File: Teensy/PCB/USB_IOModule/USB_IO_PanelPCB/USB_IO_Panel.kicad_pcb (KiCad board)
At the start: 2 copper layers, 61 x 128 mm, 31 parts, among them J1 USB_B, J2 USB_A

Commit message: Generated Gerbers
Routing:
- added copper zone on B.Cu, net shielding
- added copper zone on F.Cu, net shielding
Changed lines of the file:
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@@
       (layerselection 0x00010fc_ffffffff)
       (disableapertmacros false)
-      (usegerberextensions false)
-      (usegerberattributes true)
-      (usegerberadvancedattributes true)
-      (creategerberjobfile true)
+      (usegerberextensions true)
+      (usegerberattributes false)
+      (usegerberadvancedattributes false)
+      (creategerberjobfile false)
       (svguseinch false)
       (svgprecision 6)
@@
       (psa4output false)
       (plotreference true)
-      (plotvalue true)
+      (plotvalue false)
       (plotinvisibletext false)
       (sketchpadsonfab false)
-      (subtractmaskfromsilk false)
+      (subtractmaskfromsilk true)
       (outputformat 1)
       (mirror false)
-      (drillshape 1)
+      (drillshape 0)
       (scaleselection 1)
-      (outputdirectory "")
+      (outputdirectory "USB_IO_Panel_Gerber")
     )
   )
   (net 0 "")
+  (net 1 "shielding")
   (footprint "Potentiometer:Bourns_PTV09A-X_Hole" (layer "F.Cu")
     (at 91.435 157.48)
@@
     (fp_line (start -2.54 -64) (end 2.54 -64) (layer "User.1") (width 0.12))
     (fp_circle (center 0 0) (end 0 0) (layer "User.1") (width 0.12) (fill none))
-    (fp_line (start -1.27 -62.85) (end 1.27 -62.85) (layer "User.2") (width 0.12))
-    (fp_line (start -1.27 -59.65) (end 1.27 -59.65) (layer "User.2") (width 0.12))
-    (fp_line (start -1.27 59.65) (end 1.27 59.65) (layer "User.2") (width 0.12))
-    (fp_line (start -1.27 62.85) (end 1.27 62.85) (layer "User.2") (width 0.12))
-    (fp_arc (start -1.27 -59.65) (mid -2.87 -61.25) (end -1.27 -62.85) (layer "User.2") (width 0.12))
-    (fp_arc (start 1.27 59.65) (mid 2.87 61.25) (end 1.27 62.85) (layer "User.2") (width 0.12))
-    (fp_arc (start 1.27 -62.85) (mid 2.87 -61.25) (end 1.27 -59.65) (layer "User.2") (width 0.12))
-    (fp_arc (start -1.27 62.85) (mid -2.87 61.25) (end -1.27 59.65) (layer "User.2") (width 0.12))
-    (pad "" np_thru_hole oval (at 0 61.25) (size 5.74 3.2) (drill oval 5.74 3.2) (layers *.Mask))
-    (pad "" np_thru_hole oval (at 0 -61.25) (size 5.74 3.2) (drill oval 5.74 3.2) (layers *.Mask))
+    (fp_line (start -1.6 -59.65) (end 1.6 -59.65) (layer "User.2") (width 0.12))
+    (fp_line (start -1.6 62.85) (end 1.6 62.85) (layer "User.2") (width 0.12))
+    (fp_line (start -1.6 -62.85) (end 1.6 -62.85) (layer "User.2") (width 0.12))
+    (fp_line (start -1.6 59.65) (end 1.6 59.65) (layer "User.2") (width 0.12))
+    (fp_arc (start 1.6 -62.85) (mid 3.2 -61.25) (end 1.6 -59.65) (layer "User.2") (width 0.12))
+    (fp_arc (start -1.6 -59.65) (mid -3.2 -61.25) (end -1.6 -62.85) (layer "User.2") (width 0.12))
+    (fp_arc (start -1.6 62.85) (mid -3.2 61.25) (end -1.6 59.65) (layer "User.2") (width 0.12))
+    (fp_arc (start 1.6 59.65) (mid 3.2 61.25) (end 1.6 62.85) (layer "User.2") (width 0.12))
+    (pad "1" thru_hole oval (at 0 -61.25) (size 7.4 4.2) (drill oval 6.4 3.2) (layers *.Cu *.Mask)
+      (net 1 "shielding"))
+    (pad "1" thru_hole oval (at 0 61.25) (size 7.4 4.2) (drill oval 6.4 3.2) (layers *.Cu *.Mask)
+      (net 1 "shielding"))
   )
   (footprint "Perfboard:3.5mm Jack Perfboard_Hole" (layer "F.Cu")
@@
       (effects (font (size 1 1) (thickness 0.15)))
     )
+    (fp_line (start -2.54 64) (end 2.54 64) (layer "User.1") (width 0.12))
     (fp_line (start -2.54 -64) (end 2.54 -64) (layer "User.1") (width 0.12))
-    (fp_line (start -2.54 64) (end 2.54 64) (layer "User.1") (width 0.12))
     (fp_circle (center 0 0) (end 0 0) (layer "User.1") (width 0.12) (fill none))
-    (fp_line (start -1.27 59.65) (end 1.27 59.65) (layer "User.2") (width 0.12))
-    (fp_line (start -1.27 -62.85) (end 1.27 -62.85) (layer "User.2") (width 0.12))
-    (fp_line (start -1.27 -59.65) (end 1.27 -59.65) (layer "User.2") (width 0.12))
-    (fp_line (start -1.27 62.85) (end 1.27 62.85) (layer "User.2") (width 0.12))
-    (fp_arc (start 1.27 -62.85) (mid 2.87 -61.25) (end 1.27 -59.65) (layer "User.2") (width 0.12))
-    (fp_arc (start -1.27 -59.65) (mid -2.87 -61.25) (end -1.27 -62.85) (layer "User.2") (width 0.12))
-    (fp_arc (start -1.27 62.85) (mid -2.87 61.25) (end -1.27 59.65) (layer "User.2") (width 0.12))
-    (fp_arc (start 1.27 59.65) (mid 2.87 61.25) (end 1.27 62.85) (layer "User.2") (width 0.12))
-    (pad "" np_thru_hole oval (at 0 -61.25) (size 5.74 3.2) (drill oval 5.74 3.2) (layers *.Mask))
-    (pad "" np_thru_hole oval (at 0 61.25) (size 5.74 3.2) (drill oval 5.74 3.2) (layers *.Mask))
+    (fp_line (start -1.6 59.65) (end 1.6 59.65) (layer "User.2") (width 0.12))
+    (fp_line (start -1.6 -59.65) (end 1.6 -59.65) (layer "User.2") (width 0.12))
+    (fp_line (start -1.6 62.85) (end 1.6 62.85) (layer "User.2") (width 0.12))
+    (fp_line (start -1.6 -62.85) (end 1.6 -62.85) (layer "User.2") (width 0.12))
+    (fp_arc (start -1.6 -59.65) (mid -3.2 -61.25) (end -1.6 -62.85) (layer "User.2") (width 0.12))
+    (fp_arc (start 1.6 59.65) (mid 3.2 61.25) (end 1.6 62.85) (layer "User.2") (width 0.12))
+    (fp_arc (start -1.6 62.85) (mid -3.2 61.25) (end -1.6 59.65) (layer "User.2") (width 0.12))
+    (fp_arc (start 1.6 -62.85) (mid 3.2 -61.25) (end 1.6 -59.65) (layer "User.2") (width 0.12))
+    (pad "1" thru_hole oval (at 0 61.25) (size 7.4 4.2) (drill oval 6.4 3.2) (layers *.Cu *.Mask)
+      (net 1 "shielding"))
+    (pad "1" thru_hole oval (at 0 -61.25) (size 7.4 4.2) (drill oval 6.4 3.2) (layers *.Cu *.Mask)
+      (net 1 "shielding"))
   )
   (footprint "Perfboard:3.5mm Jack Perfboard_Hole" (layer "F.Cu")
@@
   )
   (gr_rect (start 68.58 42.68) (end 129.54 170.68) (layer "Edge.Cuts") (width 0.1) (fill none))
+  (zone (net 1) (net_name "shielding") (layers F&B.Cu) (hatch edge 0.508)
+    (connect_pads yes (clearance 0.508))
+    (min_thickness 0.254) (filled_areas_thickness no)
+    (fill yes (thermal_gap 0.508) (thermal_bridge_width 0.508))
+    (polygon
+      (pts
+        (xy 129.54 170.688)
+        (xy 68.58 170.688)
+        (xy 68.58 42.672)
+        (xy 129.54 42.672)
+      )
+    )
+  )
 )

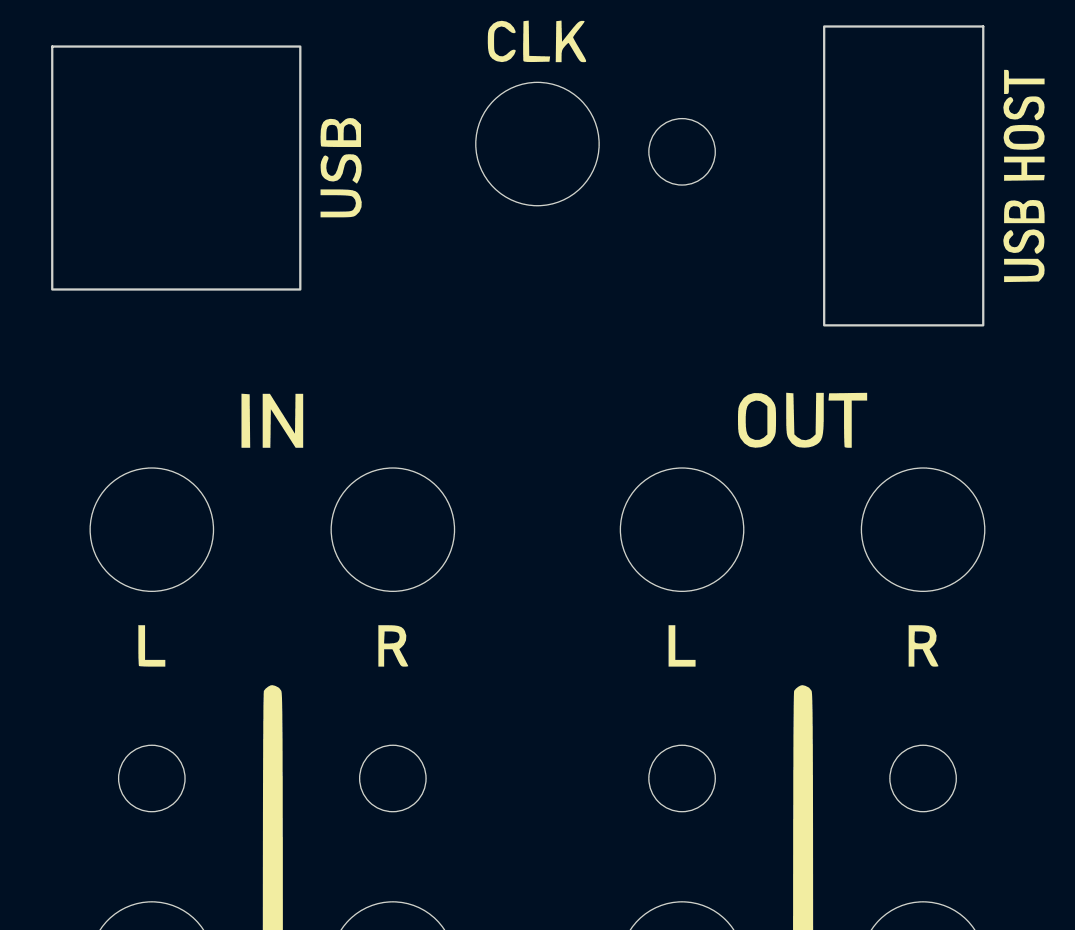
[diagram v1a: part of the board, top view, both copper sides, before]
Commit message: Added USB-C Power Supply
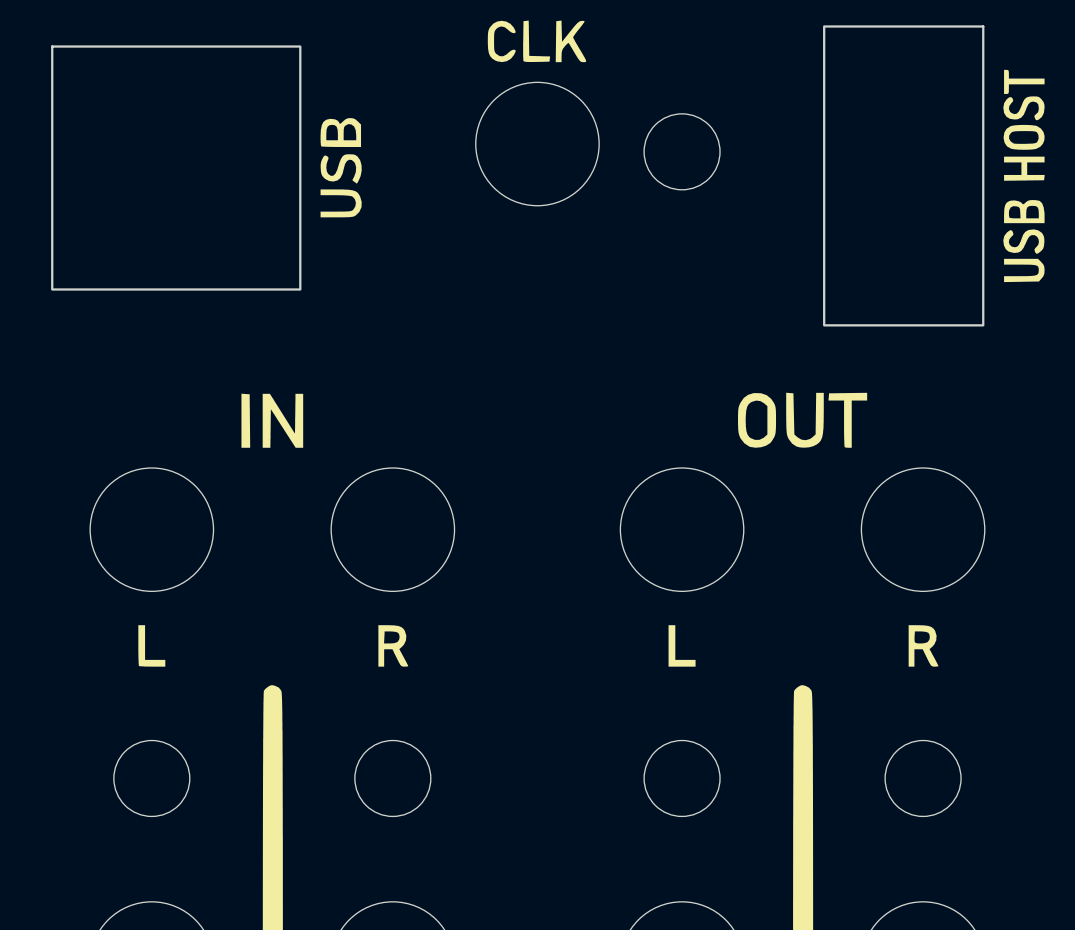
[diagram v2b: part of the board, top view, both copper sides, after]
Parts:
- D1, D2, D3, D4, D5: footprint Misc:LED_D3.0mm_Hole -> Misc:PLP5_Hole
